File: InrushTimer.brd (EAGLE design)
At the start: 62.2 x 41.3 mm, 71 parts, among them IC2 TLC272D, IC3 4076N, IC6 555, Q2 TIP41C

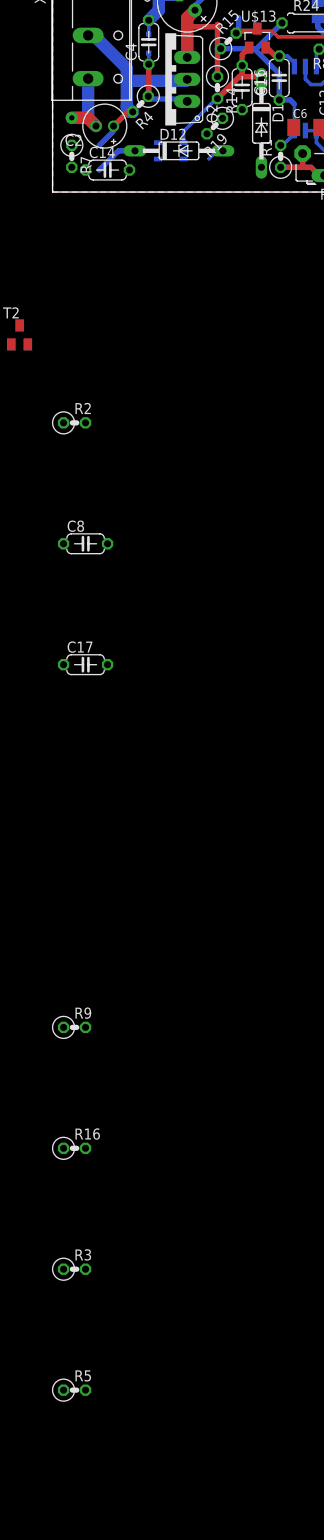
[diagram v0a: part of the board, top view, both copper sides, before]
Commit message: Added inductor model and tweaked schematic.
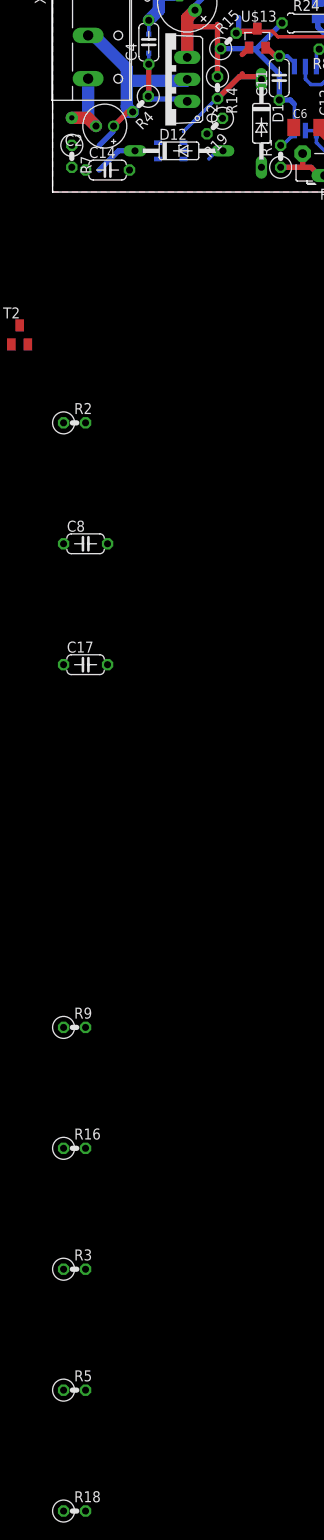
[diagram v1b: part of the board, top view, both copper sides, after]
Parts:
- removed C16: 10nF, rcl:C050-024X044
- added R18: 100, rcl:0207/2V
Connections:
- new net N$23: R18.2, U$4.1
- net RESET_N: now also R18.1; no longer C16.1, U$4.1
- net ZERO: no longer C16.2
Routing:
- net RESET_N: track 30.1 -> 25.6 mm
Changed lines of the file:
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@@
 <element name="C9" library="rcl" package="C0805K" value="1nF" x="6.6675" y="37.7825" rot="MR90"/>
 <element name="C14" library="rcl" package="C050-024X044" value="10nF" x="6.35" y="2.54"/>
-<element name="C16" library="rcl" package="C050-024X044" value="10nF" x="21.9075" y="12.065" rot="R270"/>
 <element name="C10" library="rcl" package="C0805K" value="1nF" x="13.0175" y="39.0525" rot="MR180"/>
 <element name="C1" library="rcl" package="C1206K" value="100nF" x="16.8275" y="37.465" rot="MR90"/>
@@
 <element name="R3" library="rcl" package="0207/2V" value="10K" x="2.54" y="-124.46"/>
 <element name="R5" library="rcl" package="0207/2V" value="10K" x="2.54" y="-138.43"/>
+<element name="R18" library="rcl" package="0207/2V" value="100" x="2.54" y="-152.4"/>
 </elements>
 <signals>
@@
 <contactref element="C25" pad="2"/>
 <contactref element="C9" pad="1"/>
-<contactref element="C16" pad="2"/>
 <contactref element="C1" pad="2"/>
 <contactref element="R13" pad="1"/>
@@
 <wire x1="15.1257" y1="3.8227" x2="18.05305" y2="3.8227" width="0" layer="19" extent="16-16"/>
 <wire x1="19.630525" y1="8.518025" x2="19.685" y2="4.7625" width="0" layer="19" extent="1-1"/>
-<wire x1="21.9075" y1="9.525" x2="19.630525" y2="8.518025" width="0" layer="19" extent="1-1"/>
 <wire x1="8.89" y1="2.54" x2="15.1257" y2="3.8227" width="0" layer="19" extent="16-16"/>
 <wire x1="5.0165" y1="7.62" x2="8.89" y2="2.54" width="0" layer="19" extent="16-16"/>
@@
 <wire x1="29.85135" y1="12.421871875" x2="29.21" y2="13.063221875" width="0.4064" layer="16"/>
 <wire x1="29.21" y1="13.063221875" x2="29.21" y2="14.495" width="0.4064" layer="16"/>
-<contactref element="U$4" pad="1"/>
 <contactref element="U$13" pad="1"/>
 <contactref element="D1" pad="C"/>
-<contactref element="C16" pad="1"/>
 <contactref element="R14" pad="2"/>
 <wire x1="18.923" y1="10.795" x2="15.1257" y2="6.9977" width="0.4064" layer="16"/>
@@
 <wire x1="21.59" y1="13.335" x2="23.8125" y2="13.335" width="0.6096" layer="16"/>
 <wire x1="23.8125" y1="13.335" x2="24.13" y2="13.0175" width="0.6096" layer="16"/>
-<wire x1="21.9075" y1="14.605" x2="21.9075" y2="13.6525" width="0.6096" layer="16"/>
 <wire x1="21.9075" y1="13.6525" x2="21.59" y2="13.335" width="0.6096" layer="16" curve="-90"/>
-<wire x1="15.1257" y1="6.9977" x2="15.1257" y2="5.7023" width="0.4064" layer="16"/>
 <wire x1="18.923" y1="10.795" x2="19.05" y2="10.795" width="0.4064" layer="16"/>
 <wire x1="21.59" y1="13.335" x2="19.05" y2="10.795" width="0.6096" layer="1"/>
@@
 <wire x1="21.9075" y1="13.6525" x2="21.59" y2="13.335" width="0.6096" layer="1" curve="-90"/>
 <wire x1="18.923" y1="10.795" x2="19.05" y2="10.795" width="0.4064" layer="1"/>
-<wire x1="21.9075" y1="14.605" x2="21.9075" y2="13.6525" width="0.6096" layer="1"/>
-<wire x1="21.9075" y1="14.605" x2="21.9075" y2="15.88375" width="0.6096" layer="1"/>
 <wire x1="21.9075" y1="15.88375" x2="22.70375" y2="16.68" width="0.6096" layer="1"/>
-<wire x1="24.13" y1="13.0175" x2="29.21" y2="13.063221875" width="0" layer="19" extent="16-16"/>
+<contactref element="R18" pad="1"/>
+<wire x1="15.1257" y1="6.9977" x2="1.27" y2="-152.4" width="0" layer="19" extent="16-16"/>
+<wire x1="21.9075" y1="15.88375" x2="21.9075" y2="13.6525" width="0" layer="19" extent="1-16"/>
+<wire x1="29.21" y1="13.063221875" x2="24.13" y2="13.0175" width="0" layer="19" extent="16-16"/>
 </signal>
 <signal name="HYST">
@@
 <wire x1="44.60875" y1="18.415" x2="3.81" y2="-124.46" width="0" layer="19" extent="1-1"/>
 </signal>
+<signal name="N$23">
+<contactref element="R18" pad="2"/>
+<contactref element="U$4" pad="1"/>
+<wire x1="15.1257" y1="5.7023" x2="3.81" y2="-152.4" width="0" layer="19" extent="16-16"/>
+</signal>
 </signals>

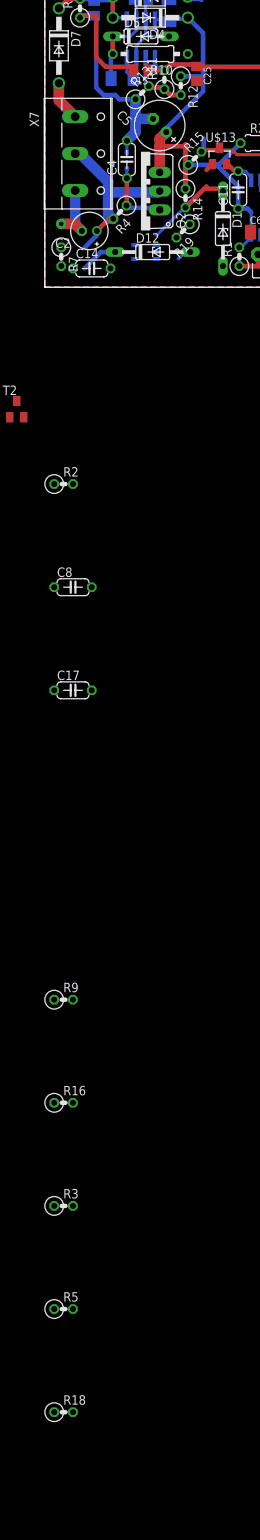
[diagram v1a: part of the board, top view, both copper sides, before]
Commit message: Updated values and topology on schematic.
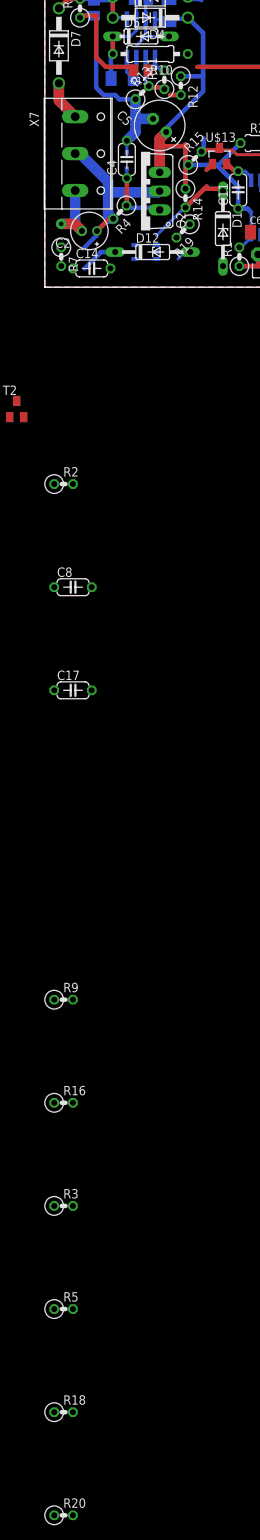
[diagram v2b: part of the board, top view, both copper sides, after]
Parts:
- removed C25: 10p, rcl:C0805K
- added R20: 10K, rcl:0207/2V
- C15: value 10p -> 10p (DNF)
- C17, C8: value 100nF -> 100nF (DNF)
- C9: value 1nF -> 10nF
- R12: value 43K -> 200K
- R13: value 10K -> 100K
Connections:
- new net N$26: IC2.3, R11.1, R20.2
- net HYST: no longer R11.1
- net N$7: now also R20.1; no longer IC2.3
- net PEAK: no longer C25.1
- net ZERO: no longer C25.2
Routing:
- net PEAK: track 34.7 -> 27.2 mm
- net HYST: track 14.4 -> 11.9 mm
- net N$7: track 12.1 -> 10.4 mm
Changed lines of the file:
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@@
 <element name="R10" library="rcl" package="0207/10" value="9.1M" x="14.2875" y="31.59125" rot="R180"/>
 <element name="D5" library="diode" package="DO35-7" value="1N4148DO35-7" x="13.0175" y="33.9725"/>
-<element name="R12" library="rcl" package="0207/2V" value="43K" x="18.415" y="27.305" rot="R270"/>
-<element name="R13" library="rcl" package="0207/2V" value="10K" x="13.17625" y="26.3525" rot="R45"/>
+<element name="R12" library="rcl" package="0207/2V" value="200K" x="18.415" y="27.305" rot="R270"/>
+<element name="R13" library="rcl" package="0207/2V" value="100K" x="13.17625" y="26.3525" rot="R45"/>
 <element name="IC3" library="40xx" package="DIL16" value="4076N" x="40.79875" y="22.225" rot="R90"/>
 <element name="D6" library="diode" package="DO41-10" value="1n4001" x="14.2875" y="39.37"/>
@@
 <element name="R14" library="rcl" package="0207/2V" value="22K" x="19.05" y="12.065" rot="R270"/>
 <element name="R19" library="rcl" package="0207/2V" value="10K" x="18.7325" y="7.62" rot="R225"/>
-<element name="C15" library="rcl" package="C0805K" value="10p" x="13.0175" y="29.36875" rot="R180"/>
+<element name="C15" library="rcl" package="C0805K" value="10p (DNF)" x="13.0175" y="29.36875" rot="R180"/>
 <element name="U$3" library="transistor-fet" package="SOT23" value="2N7002" x="43.4975" y="8.89" rot="MR90"/>
 <element name="D12" library="diode" package="DO35Z10" value="BZX55" x="14.605" y="4.7625"/>
@@
 <element name="C4" library="rcl" package="C050-024X044" value="100nF" x="11.1125" y="17.30375" rot="R90"/>
 <element name="C13" library="rcl" package="C1206K" value="100nF" x="10.4775" y="28.2575" rot="MR180"/>
-<element name="C25" library="rcl" package="C0805K" value="10p" x="20.6375" y="28.8925" rot="R270"/>
 <element name="U$5" library="SHoleLib" package="FODM" value="FODM3053" x="51.435" y="36.5125" rot="MR90"/>
 <element name="Q2" library="transistor-power" package="TO220AV" value="TIP41C" x="13.0175" y="13.0175" rot="R90"/>
@@
 <attribute name="MF" value="" x="56.8325" y="36.195" size="1.778" layer="27" rot="R90" display="off"/>
 </element>
-<element name="C9" library="rcl" package="C0805K" value="1nF" x="6.6675" y="37.7825" rot="MR90"/>
+<element name="C9" library="rcl" package="C0805K" value="10nF" x="6.6675" y="37.7825" rot="MR90"/>
 <element name="C14" library="rcl" package="C050-024X044" value="10nF" x="6.35" y="2.54"/>
 <element name="C10" library="rcl" package="C0805K" value="1nF" x="13.0175" y="39.0525" rot="MR180"/>
@@
 <element name="T2" library="transistor" package="SOT23-BEC" value="" x="-3.81" y="-16.51"/>
 <element name="R2" library="rcl" package="0207/2V" value="10K" x="2.54" y="-26.67"/>
-<element name="C8" library="rcl" package="C050-024X044" value="100nF" x="3.81" y="-40.64"/>
-<element name="C17" library="rcl" package="C050-024X044" value="100nF" x="3.81" y="-54.61"/>
+<element name="C8" library="rcl" package="C050-024X044" value="100nF (DNF)" x="3.81" y="-40.64"/>
+<element name="C17" library="rcl" package="C050-024X044" value="100nF (DNF)" x="3.81" y="-54.61"/>
 <element name="R9" library="rcl" package="0207/2V" value="10K" x="2.54" y="-96.52"/>
 <element name="R16" library="rcl" package="0207/2V" value="10K" x="2.54" y="-110.49"/>
@@
 <element name="R5" library="rcl" package="0207/2V" value="10K" x="2.54" y="-138.43"/>
 <element name="R18" library="rcl" package="0207/2V" value="100" x="2.54" y="-152.4"/>
+<element name="R20" library="rcl" package="0207/2V" value="10K" x="2.54" y="-166.37"/>
 </elements>
 <signals>
@@
 <contactref element="C15" pad="2"/>
 <contactref element="C13" pad="2"/>
-<contactref element="C25" pad="2"/>
 <contactref element="C9" pad="1"/>
 <contactref element="C1" pad="2"/>
@@
 <wire x1="11.1125" y1="29.1225" x2="12.0175" y2="29.36875" width="0" layer="19" extent="1-16"/>
 <wire x1="19.3675" y1="31.59125" x2="12.0175" y2="29.845" width="0" layer="19" extent="1-1"/>
-<wire x1="20.6375" y1="27.8925" x2="19.3675" y2="31.59125" width="0" layer="19" extent="1-1"/>
 <wire x1="19.68309375" y1="39.05440625" x2="19.3675" y2="31.59125" width="0" layer="19" extent="16-16"/>
 <wire x1="1.27" y1="-26.67" x2="8.89" y2="2.54" width="0" layer="19" extent="1-1"/>
@@
 <signal name="PEAK">
 <contactref element="IC3" pad="7"/>
-<contactref element="R11" pad="2"/>
 <contactref element="C15" pad="1"/>
-<contactref element="C25" pad="1"/>
 <contactref element="IC2" pad="1"/>
 <wire x1="14.9225" y1="31.055" x2="14.9225" y2="30.140275" width="0.4064" layer="16"/>
 <wire x1="14.9225" y1="30.140275" x2="15.653384375" y2="29.409390625" width="0.4064" layer="16"/>
 <wire x1="15.653384375" y1="29.409390625" x2="16.151859375" y2="29.409390625" width="0.4064" layer="16"/>
-<wire x1="16.151859375" y1="29.409390625" x2="16.1925" y2="29.36875" width="0.4064" layer="16"/>
 <wire x1="14.224" y1="29.464" x2="14.0175" y2="29.36875" width="0.6096" layer="1"/>
-<wire x1="16.256" y1="29.464" x2="16.1925" y2="29.36875" width="0.6096" layer="16"/>
 <wire x1="44.32935" y1="28.8544" x2="43.69435" y2="28.8544" width="0.4064" layer="1"/>
 <wire x1="43.69435" y1="28.8544" x2="42.70375" y2="29.845" width="0.4064" layer="1"/>
 <wire x1="44.60875" y1="28.575" x2="44.32935" y2="28.8544" width="0.4064" layer="1"/>
-<wire x1="16.1925" y1="29.36875" x2="14.0175" y2="29.36875" width="0.6096" layer="1"/>
-<wire x1="20.6375" y1="30.1625" x2="20.3675" y2="30.1625" width="0.6096" layer="1"/>
-<wire x1="20.32" y1="30.1625" x2="16.98625" y2="30.1625" width="0.6096" layer="1"/>
-<wire x1="16.98625" y1="30.1625" x2="16.1925" y2="29.36875" width="0.6096" layer="1"/>
 <wire x1="42.70375" y1="29.845" x2="34.925" y2="29.845" width="0.4064" layer="1"/>
 <wire x1="34.925" y1="29.845" x2="20.6375" y2="29.845" width="0.6096" layer="1"/>
-<wire x1="20.6375" y1="29.845" x2="20.6375" y2="29.8925" width="0.6096" layer="1"/>
-<wire x1="20.6375" y1="29.8925" x2="20.3675" y2="30.1625" width="0.6096" layer="1"/>
-<wire x1="20.3675" y1="30.1625" x2="20.32" y2="30.1625" width="0.6096" layer="1"/>
+<contactref element="R11" pad="2"/>
+<wire x1="16.1925" y1="29.36875" x2="20.6375" y2="29.845" width="0" layer="19" extent="1-1"/>
+<wire x1="16.151859375" y1="29.409390625" x2="16.1925" y2="29.36875" width="0" layer="19" extent="16-16"/>
+<wire x1="14.224" y1="29.464" x2="14.9225" y2="30.140275" width="0" layer="19" extent="1-16"/>
 </signal>
 <signal name="N$16">
@@
 </signal>
 <signal name="HYST">
-<contactref element="R11" pad="1"/>
 <contactref element="IC2" pad="2"/>
 <contactref element="R13" pad="2"/>
@@
 <wire x1="13.6525" y1="27.250525" x2="14.074275" y2="27.250525" width="0.4064" layer="16"/>
 <wire x1="18.415" y1="26.035" x2="16.98625" y2="26.035" width="0.6096" layer="16"/>
-<wire x1="16.98625" y1="26.035" x2="16.1925" y2="26.82875" width="0.6096" layer="16"/>
-<wire x1="16.1925" y1="26.82875" x2="16.1925" y2="26.944321875" width="0.6096" layer="16"/>
 <wire x1="16.1925" y1="26.944321875" x2="16.28584375" y2="27.037665625" width="0.6096" layer="16"/>
 <wire x1="16.28584375" y1="27.037665625" x2="14.287134375" y2="27.037665625" width="0.6096" layer="16"/>
 <wire x1="14.287134375" y1="27.037665625" x2="14.074275" y2="27.250525" width="0.6096" layer="16"/>
 <wire x1="18.415" y1="26.035" x2="16.98625" y2="26.035" width="0.6096" layer="1"/>
-<wire x1="16.98625" y1="26.035" x2="16.1925" y2="26.82875" width="0.6096" layer="1"/>
-<wire x1="16.1925" y1="26.82875" x2="16.1925" y2="26.944321875" width="0.6096" layer="1"/>
 <wire x1="16.1925" y1="26.944321875" x2="16.28584375" y2="27.037665625" width="0.6096" layer="1"/>
 <wire x1="16.28584375" y1="27.037665625" x2="14.287134375" y2="27.037665625" width="0.6096" layer="1"/>
 <wire x1="14.287134375" y1="27.037665625" x2="14.074275" y2="27.250525" width="0.6096" layer="1"/>
+<wire x1="16.1925" y1="26.944321875" x2="16.98625" y2="26.035" width="0" layer="19" extent="16-16"/>
 </signal>
 <signal name="N$11">
@@
 </signal>
 <signal name="N$7">
-<contactref element="IC2" pad="3"/>
 <contactref element="D5" pad="A"/>
 <contactref element="C10" pad="2"/>
@@
 <wire x1="13.6525" y1="36.255" x2="13.6525" y2="33.9725" width="0.4064" layer="16"/>
 <wire x1="13.6525" y1="33.9725" x2="12.3825" y2="32.7025" width="0.4064" layer="16"/>
-<wire x1="12.3825" y1="32.7025" x2="12.3825" y2="31.055" width="0.4064" layer="16"/>
 <wire x1="14.0175" y1="39.0525" x2="13.6525" y2="39.0525" width="0.4064" layer="16"/>
 <wire x1="13.6525" y1="39.0525" x2="13.6525" y2="36.255" width="0.4064" layer="16"/>
 <contactref element="C7" pad="2"/>
-<wire x1="13.6525" y1="39.0525" x2="13.7" y2="40.64" width="0" layer="19" extent="1-16"/>
+<contactref element="R20" pad="1"/>
+<wire x1="12.3825" y1="32.7025" x2="1.27" y2="-166.37" width="0" layer="19" extent="16-16"/>
+<wire x1="13.7" y1="40.64" x2="13.6525" y2="39.0525" width="0" layer="19" extent="1-16"/>
 </signal>
 <signal name="N$28">
@@
 <wire x1="15.1257" y1="5.7023" x2="3.81" y2="-152.4" width="0" layer="19" extent="16-16"/>
 </signal>
+<signal name="N$26">
+<contactref element="R20" pad="2"/>
+<contactref element="IC2" pad="3"/>
+<contactref element="R11" pad="1"/>
+<wire x1="16.1925" y1="26.82875" x2="3.81" y2="-166.37" width="0" layer="19" extent="1-1"/>
+<wire x1="12.3825" y1="31.055" x2="16.1925" y2="26.82875" width="0" layer="19" extent="16-16"/>
+</signal>
 </signals>

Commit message: Corrected component values (units)
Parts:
- C15: value 10p (DNF) -> 10pF (DNF)
- C2: value 10u -> 10uF
- C5: value 100u -> 100uF
- R18: value 100 -> 100R
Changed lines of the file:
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@@
 <elements>
 <element name="D3" library="diode" package="SOD323-R" value="Z12V" x="11.1125" y="17.145" rot="MR90"/>
-<element name="C2" library="rcl" package="E2-5" value="10u" x="6.0325" y="7.62" rot="R180"/>
-<element name="C5" library="rcl" package="E2,5-7" value="100u" x="15.5575" y="21.9075" rot="R135"/>
+<element name="C2" library="rcl" package="E2-5" value="10uF" x="6.0325" y="7.62" rot="R180"/>
+<element name="C5" library="rcl" package="E2,5-7" value="100uF" x="15.5575" y="21.9075" rot="R135"/>
 <element name="R4" library="rcl" package="0207/2V" value="4K7" x="10.16" y="10.16" rot="R225"/>
 <element name="R6" library="rcl" package="0207/2V" value="22K" x="4.7625" y="37.7825" rot="R90"/>
@@
 <element name="R14" library="rcl" package="0207/2V" value="22K" x="19.05" y="12.065" rot="R270"/>
 <element name="R19" library="rcl" package="0207/2V" value="10K" x="18.7325" y="7.62" rot="R225"/>
-<element name="C15" library="rcl" package="C0805K" value="10p (DNF)" x="13.0175" y="29.36875" rot="R180"/>
+<element name="C15" library="rcl" package="C0805K" value="10pF (DNF)" x="13.0175" y="29.36875" rot="R180"/>
 <element name="U$3" library="transistor-fet" package="SOT23" value="2N7002" x="43.4975" y="8.89" rot="MR90"/>
 <element name="D12" library="diode" package="DO35Z10" value="BZX55" x="14.605" y="4.7625"/>
@@
 <element name="R3" library="rcl" package="0207/2V" value="10K" x="2.54" y="-124.46"/>
 <element name="R5" library="rcl" package="0207/2V" value="10K" x="2.54" y="-138.43"/>
-<element name="R18" library="rcl" package="0207/2V" value="100" x="2.54" y="-152.4"/>
+<element name="R18" library="rcl" package="0207/2V" value="100R" x="2.54" y="-152.4"/>
 <element name="R20" library="rcl" package="0207/2V" value="10K" x="2.54" y="-166.37"/>
 </elements>
